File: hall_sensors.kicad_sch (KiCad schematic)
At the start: 192 parts, among them U401 UHE4913, U402 UHE4913, U403 UHE4913, U404 UHE4913, U405 UHE4913, U406 UHE4913, U407 UHE4913, U408 UHE4913, U409 UHE4913, U410 UHE4913, U411 UHE4913, U412 UHE4913, U413 UHE4913, U414 UHE4913, U415 UHE4913, U416 UHE4913, U417 UHE4913, U418 UHE4913, U419 UHE4913, U420 UHE4913, U421 UHE4913, U422 UHE4913, U423 UHE4913, U424 UHE4913, U425 UHE4913, U426 UHE4913, U427 UHE4913, U428 UHE4913, U429 UHE4913, U430 UHE4913, U431 UHE4913, U432 UHE4913, U433 UHE4913, U434 UHE4913, U435 UHE4913, U436 UHE4913, U437 UHE4913, U438 UHE4913, U439 UHE4913, U440 UHE4913, U441 UHE4913, U442 UHE4913, U443 UHE4913, U444 UHE4913, U445 UHE4913, U446 UHE4913, U447 UHE4913, U448 UHE4913, U449 UHE4913, U450 UHE4913, U451 UHE4913, U452 UHE4913, U453 UHE4913, U454 UHE4913, U455 UHE4913, U456 UHE4913, U457 UHE4913, U458 UHE4913, U459 UHE4913, U460 UHE4913, U461 UHE4913, U462 UHE4913, U463 UHE4913, U464 UHE4913

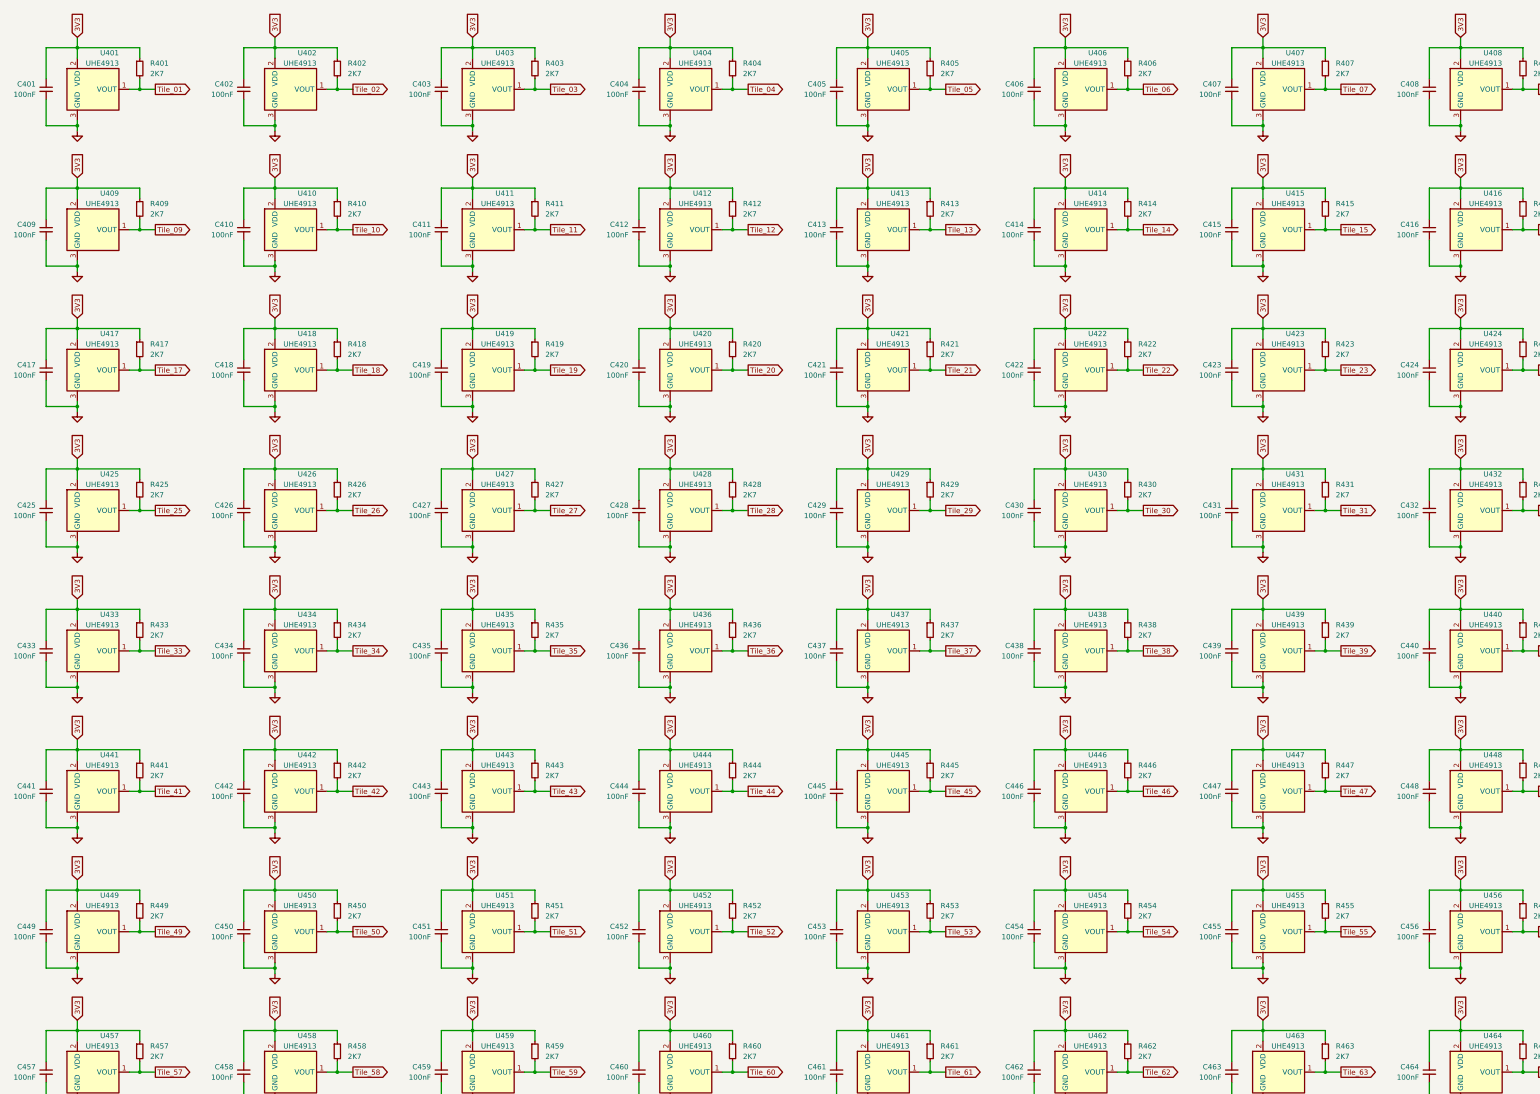
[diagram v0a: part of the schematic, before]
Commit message: update hierarchical labels
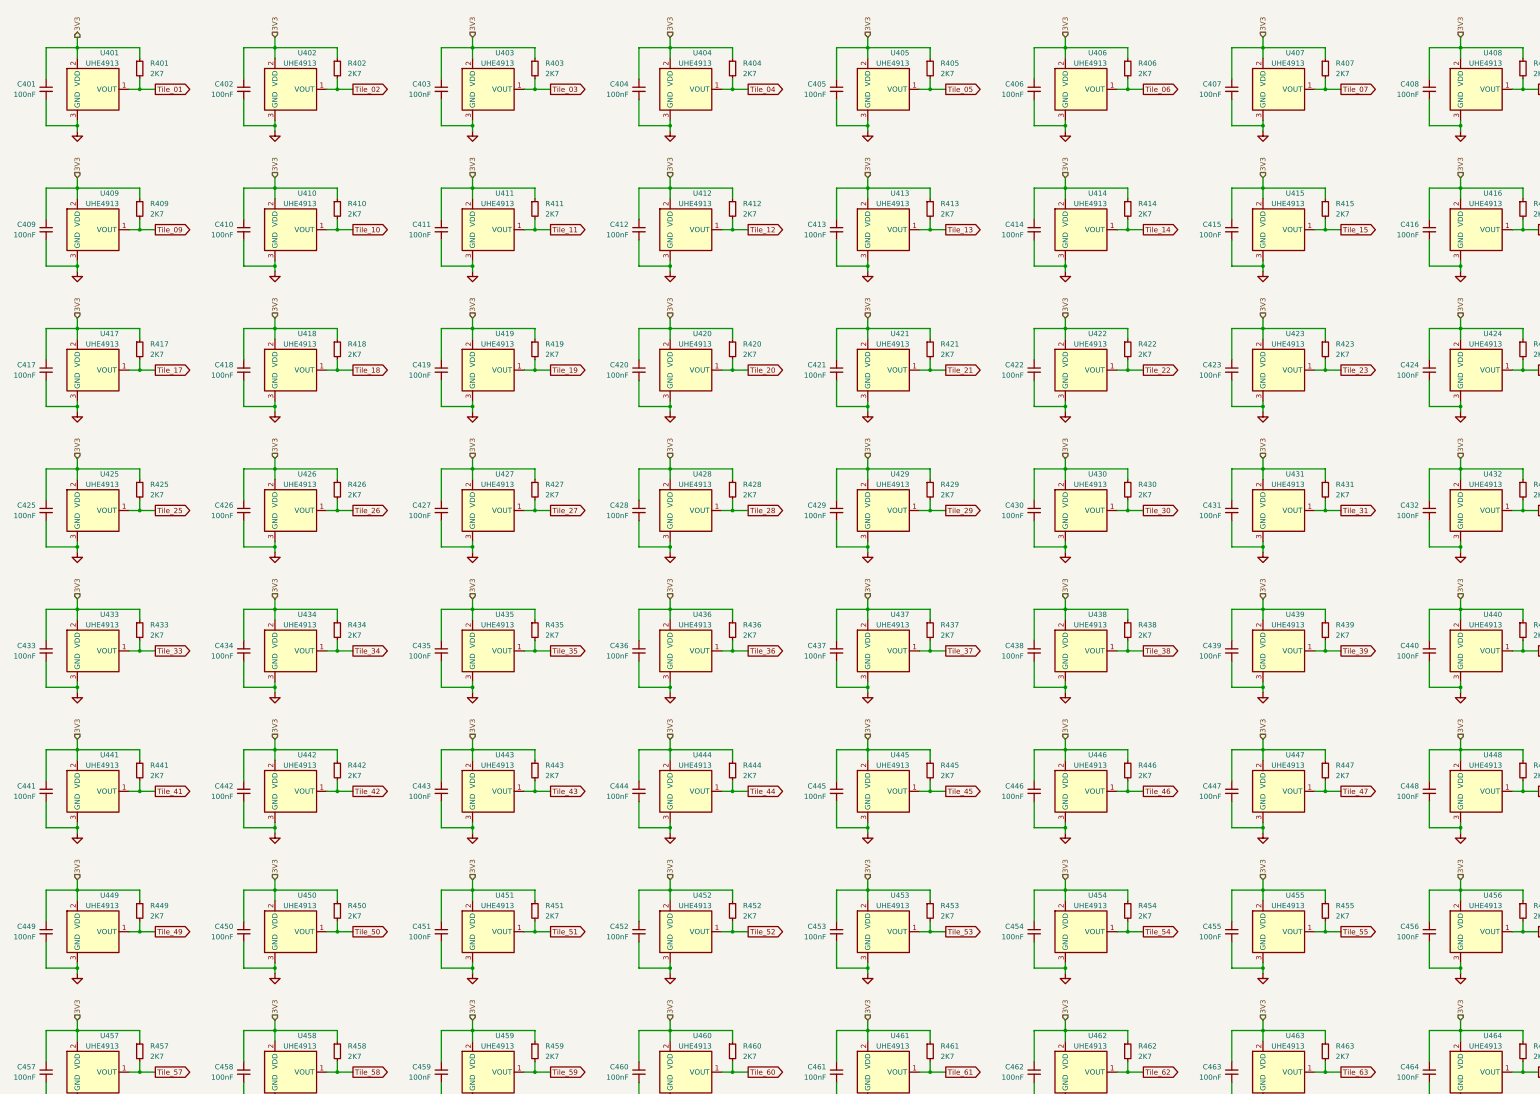
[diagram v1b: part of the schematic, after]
